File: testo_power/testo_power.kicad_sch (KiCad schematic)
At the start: 0 parts

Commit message: Test commit for KiCad schemes
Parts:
- added J1: USB_C_Receptacle_PowerOnly_6P, symbol Connector:USB_C_Receptacle_PowerOnly_6P
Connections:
- new net: J1.A12 (GND), J1.B12 (GND)
- new net: J1.A9 (VBUS), J1.B9 (VBUS)
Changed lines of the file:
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@@
 (kicad_sch
-	(version 20250114)
+	(version 20260306)
 	(generator "eeschema")
-	(generator_version "9.0")
+	(generator_version "10.0")
 	(paper "A4")
+	(symbol
+		(lib_id "Connector:USB_C_Receptacle_PowerOnly_6P")
+		(at 74.93 71.12 0)
+		(unit 1)
+		(body_style 1)
+		(exclude_from_sim no)
+		(in_bom yes)
+		(on_board yes)
+		(in_pos_files yes)
+		(dnp no)
+		(fields_autoplaced yes)
+		(property "Reference" "J1"
+			(at 74.93 53.34 0)
+			(show_name no)
+			(do_not_autoplace no)
+			(effects
+				(font
+					(size 1.27 1.27)
+				)
+			)
+		)
+		(property "Value" "USB_C_Receptacle_PowerOnly_6P"
+			(at 74.93 55.88 0)
+			(show_name no)
+			(do_not_autoplace no)
+			(effects
+				(font
+					(size 1.27 1.27)
+				)
+			)
+		)
+		(property "Footprint" ""
+			(at 78.74 68.58 0)
+			(hide yes)
+			(show_name no)
+			(do_not_autoplace no)
+			(effects
+				(font
+					(size 1.27 1.27)
+				)
+			)
+		)
+		(property "Datasheet" "https://www.usb.org/sites/default/files/documents/usb_type-c.zip"
+			(at 74.93 71.12 0)
+			(hide yes)
+			(show_name no)
+			(do_not_autoplace no)
+			(effects
+				(font
+					(size 1.27 1.27)
+				)
+			)
+		)
+		(property "Description" "USB Power-Only 6P Type-C Receptacle connector"
+			(at 74.93 71.12 0)
+			(hide yes)
+			(show_name no)
+			(do_not_autoplace no)
+			(effects
+				(font
+					(size 1.27 1.27)
+				)
+			)
+		)
+		(pin "B5"
+		)
+		(pin "A9"
+		)
+		(pin "SH"
+		)
+		(pin "A5"
+		)
+		(pin "B12"
+		)
+		(pin "A12"
+		)
+		(pin "B9"
+		)
+		(instances
+			(project "testo_power"
+				(path "/7d8517b7-4e53-4e94-8436-66e52bec9654"
+					(reference "J1")
+					(unit 1)
+				)
+			)
+		)
+	)
 	(sheet_instances
 		(path "/"

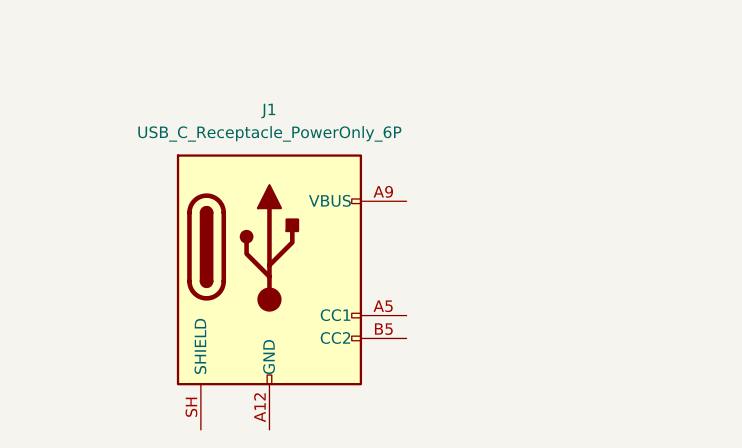
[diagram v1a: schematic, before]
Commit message: First schematic drawing
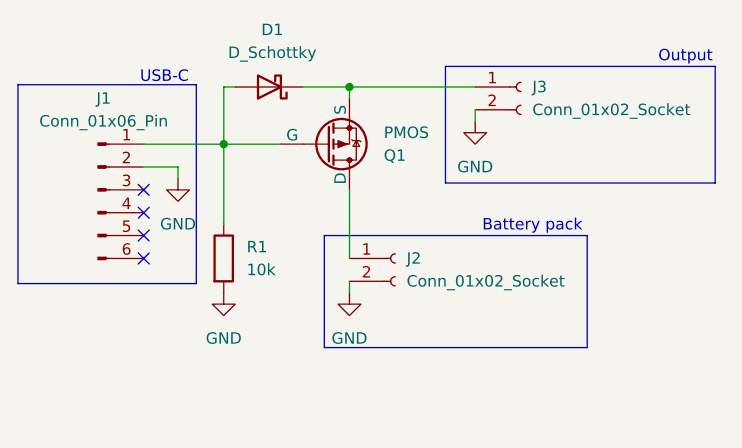
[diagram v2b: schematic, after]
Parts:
- removed J1: USB_C_Receptacle_PowerOnly_6P, symbol Connector:USB_C_Receptacle_PowerOnly_6P
- added D1: D_Schottky, symbol Device:D_Schottky
- added J1: Conn_01x06_Pin, symbol Connector:Conn_01x06_Pin
- added J2, J3: Conn_01x02_Socket, symbol Connector:Conn_01x02_Socket
- added Q1: PMOS, symbol Simulation_SPICE:PMOS
- added R1: 10k, symbol Device:R
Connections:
- new net: D1.2 (A), J1.1 (Pin_1), Q1.2 (G), R1.1
- new net: D1.1 (K), J3.1 (Pin_1), Q1.3 (S)
- new net: J2.1 (Pin_1), Q1.1 (D)
- new net GND: J1.2 (Pin_2), J2.2 (Pin_2), J3.2 (Pin_2), R1.2
- no-connect marks 0 -> 4
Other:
- note added: "Battery pack"
- note added: "Output"
- note added: "USB-C"

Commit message: First version of PCB design
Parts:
- removed Q1: PMOS, symbol Simulation_SPICE:PMOS
- added Q2: FQP27P06, Package_TO_SOT_THT:TO-220-3_Vertical, symbol Transistor_FET:FQP27P06
- D1: footprint (none) -> Diode_THT:D_5W_P10.16mm_Horizontal
- J1: footprint (none) -> Connector_PinHeader_2.54mm:PinHeader_1x06_P2.54mm_Vertical
- J2: footprint (none) -> Connector_Molex:Molex_KK-254_AE-6410-02A_1x02_P2.54mm_Vertical
- J3: footprint (none) -> Connector_PinHeader_2.54mm:PinHeader_1x02_P2.54mm_Vertical
- R1: footprint (none) -> Resistor_THT:R_Axial_DIN0207_L6.3mm_D2.5mm_P7.62mm_Horizontal
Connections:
- net V_USB: now reaches D1.2 (A), J1.1 (Pin_1), R1.1
- net V_USB: now also Q2.1 (G)
- net V_OUT: now reaches D1.1 (K), J3.1 (Pin_1)
- net V_OUT: now also Q2.3 (S)
- net V_BAT: now reaches J2.1 (Pin_1)
- net V_BAT: now also Q2.2 (D)
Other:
- moved on the sheet: J3

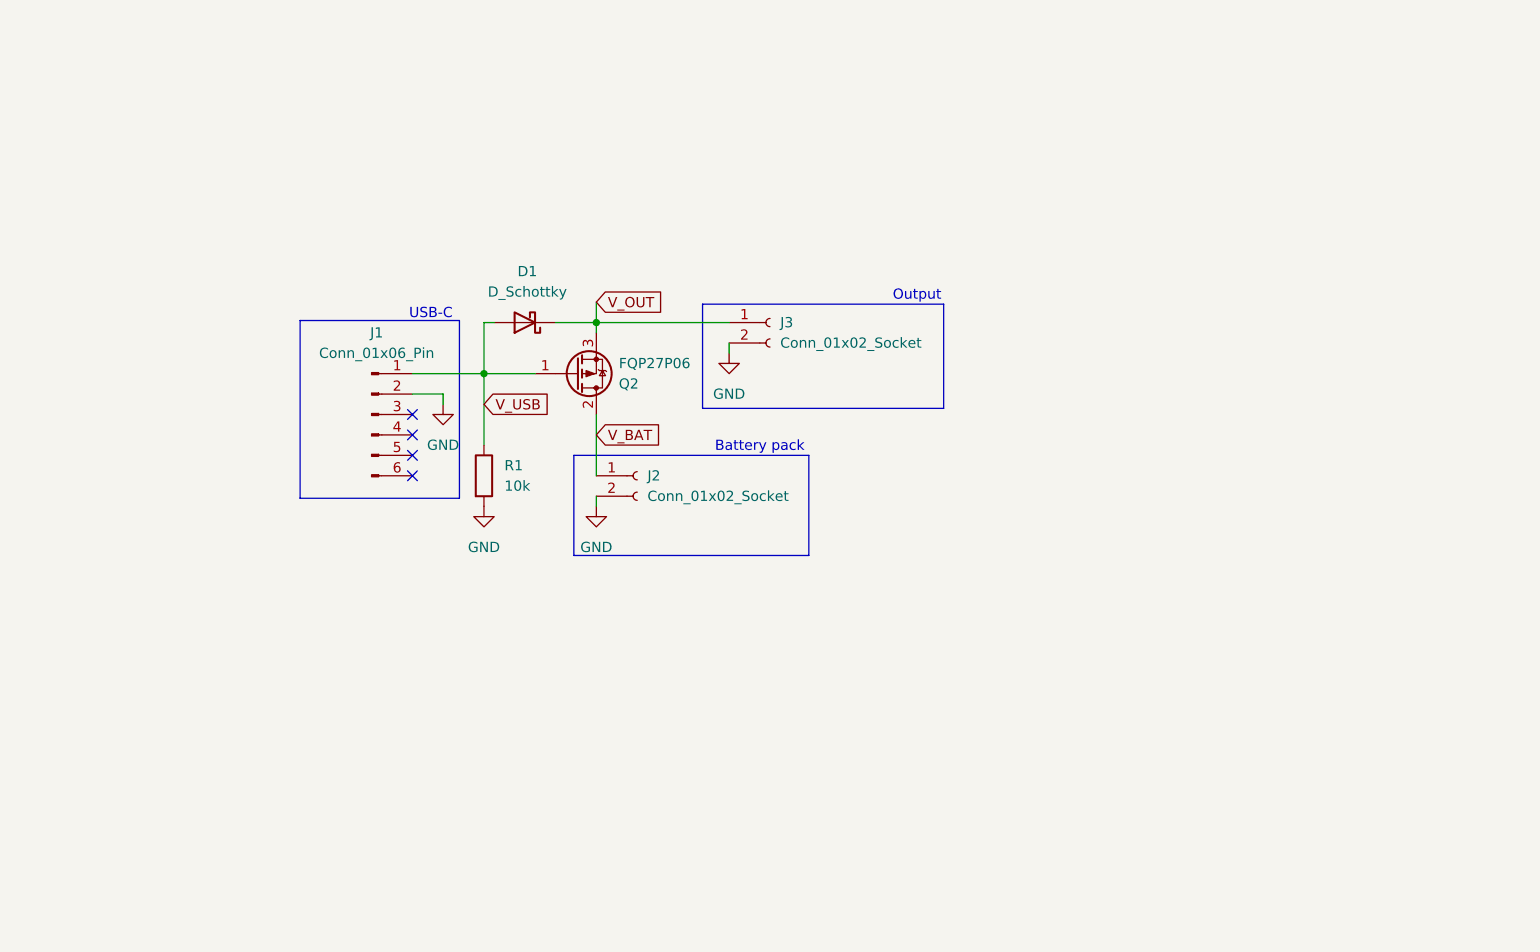
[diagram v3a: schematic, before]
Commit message: Added mounting holes, added descriptions on silkscreen, added USB power indication LED.
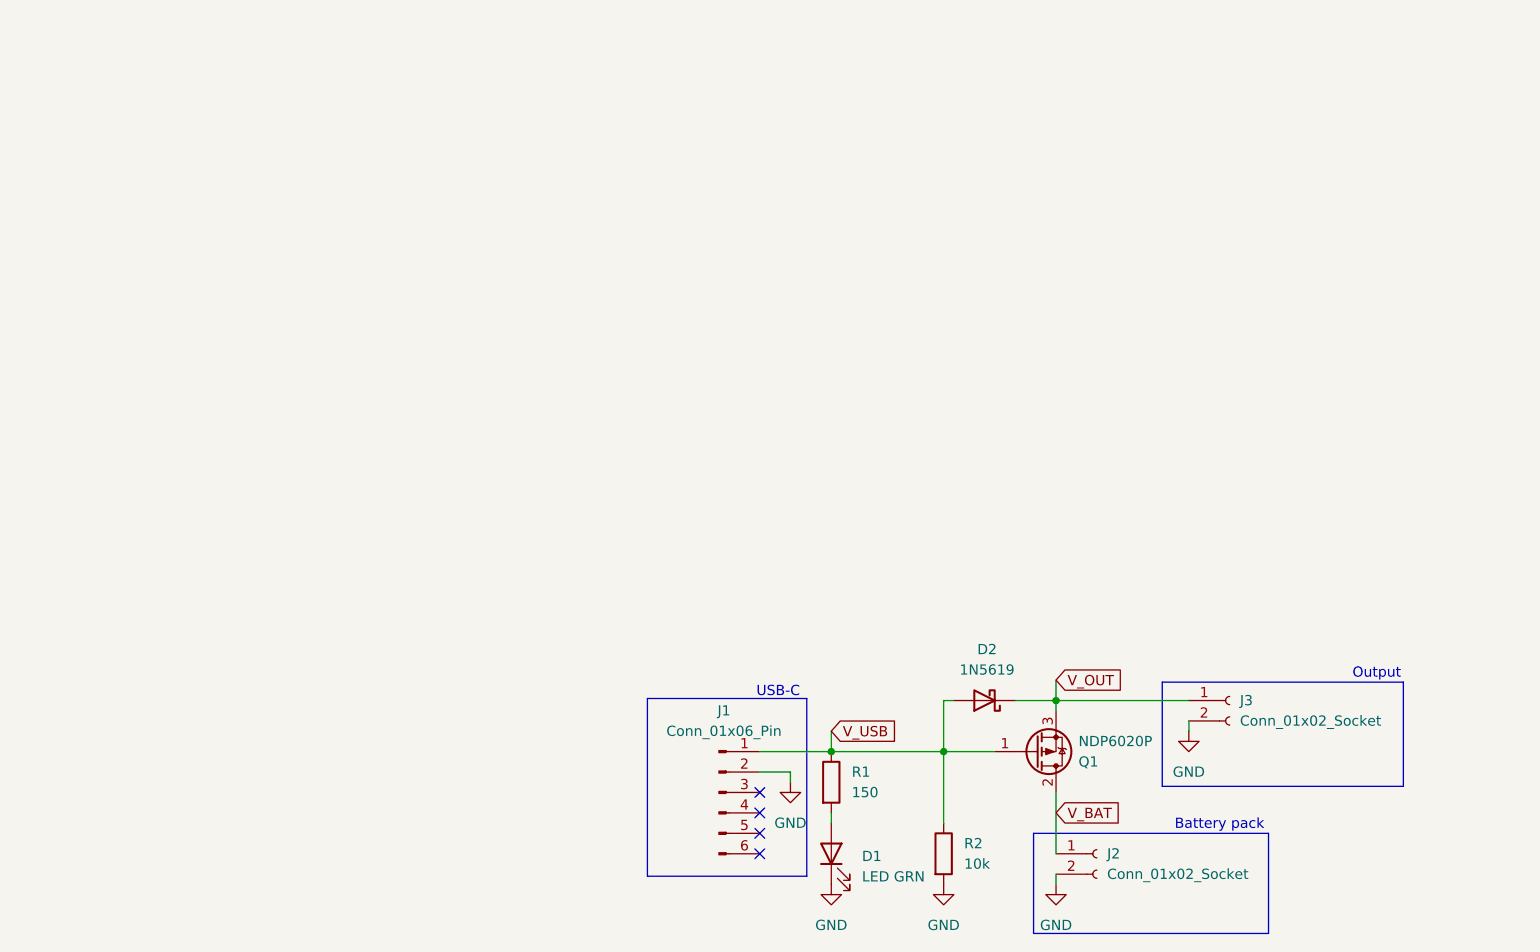
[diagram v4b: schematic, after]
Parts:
- added D1: LED GRN, LED_THT:LED_D4.0mm, symbol Device:LED
- added R1: 150, Resistor_THT:R_Axial_DIN0207_L6.3mm_D2.5mm_P7.62mm_Horizontal, symbol Device:R
- D2: renamed from D1; value D_Schottky -> 1N5619
- Q1: renamed from Q2; value FQP27P06 -> NDP6020P
- renumbered R1 to R2
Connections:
- net GND: now also D1.1 (K)
- net V_USB: now also R1.1
- new net: D1.2 (A), R1.2
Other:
- company: (none) -> Hogeschool Utrecht
- title: (none) -> Testo USB-C mod
- moved on the sheet: D2, J1, J2, J3, Q1, R2

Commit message: pcb and schematic done
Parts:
- removed J1: Conn_01x06_Pin, Connector_PinHeader_2.54mm:PinHeader_1x06_P2.54mm_Vertical, symbol Connector:Conn_01x06_Pin
- removed Q1: NDP6020P, Package_TO_SOT_THT:TO-220-3_Vertical, symbol Transistor_FET:FQP27P06
- added J1: USB_C_Receptacle_PowerOnly_6P, Connector_USB:USB_C_Receptacle_HCTL_HC-TYPE-C-16P-01A, symbol Connector:USB_C_Receptacle_PowerOnly_6P
- added Q2: IRLML6402TRPBF, Package_TO_SOT_SMD:SOT-23, symbol Transistor_FET:Q_PMOS_GSD
- added R3: 150R, Resistor_SMD:R_0603_1608Metric, symbol Device:R
- added R4: 10k, Resistor_SMD:R_0603_1608Metric, symbol Device:R
- D1: value LED GRN -> LED RED; footprint LED_THT:LED_D4.0mm -> LED_SMD:LED_0603_1608Metric; JLC Part# (none) -> C2286
- D2: value 1N5619 -> SS14; footprint Diode_THT:D_5W_P10.16mm_Horizontal -> Diode_SMD:D_SMA; JLC Part# (none) -> C2480
- J2: footprint Connector_Molex:Molex_KK-254_AE-6410-02A_1x02_P2.54mm_Vertical -> Connector_Molex:Molex_CLIK-Mate_502382-0270_1x02-1MP_P1.25mm_Vertical; JLC Part# (none) -> C27543
- J3: footprint Connector_PinHeader_2.54mm:PinHeader_1x02_P2.54mm_Vertical -> Connector_Molex:Molex_KK-254_AE-6410-02A_1x02_P2.54mm_Vertical; JLC Part# (none) -> C27543
- R1: value 150 -> 5k1; footprint Resistor_THT:R_Axial_DIN0207_L6.3mm_D2.5mm_P7.62mm_Horizontal -> Resistor_SMD:R_0603_1608Metric; JLC Part# (none) -> C23186
- R2: value 10k -> 5k1; footprint Resistor_THT:R_Axial_DIN0207_L6.3mm_D2.5mm_P7.62mm_Horizontal -> Resistor_SMD:R_0603_1608Metric; JLC Part# (none) -> C23186
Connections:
- net GND: now also R1.1, R2.1, J1.A12 (GND), J1.B12 (GND), J1.SH (SHIELD), R4.2; no longer R2.2
- net V_BAT: now also J3.1 (Pin_1), Q2.2 (S); no longer J2.1 (Pin_1)
- net V_OUT: now also J2.1 (Pin_1), Q2.3 (D); no longer J3.1 (Pin_1)
- net at D1.2 (A): now also R3.2; no longer R1.2
- removed net V_USB: D2.2 (A), R1.1, R2.1
- new net: J1.A5 (CC1), R2.2
- new net: J1.B5 (CC2), R1.2
- new net V_BUS: D2.2 (A), J1.A9 (VBUS), J1.B9 (VBUS), Q2.1 (G), R3.1, R4.1
- no-connect marks 4 -> 0
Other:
- note removed: "USB-C"

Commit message: replaced connectors
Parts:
- J2: footprint Connector_Molex:Molex_CLIK-Mate_502382-0270_1x02-1MP_P1.25mm_Vertical -> Connector_PinHeader_2.54mm:PinHeader_1x02_P2.54mm_Vertical; JLC Part# C27543 -> (none)
- J3: footprint Connector_Molex:Molex_KK-254_AE-6410-02A_1x02_P2.54mm_Vertical -> Connector_Molex:Molex_CLIK-Mate_502382-0270_1x02-1MP_P1.25mm_Vertical
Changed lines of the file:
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@@
 			)
 		)
-		(property "Footprint" "Connector_Molex:Molex_CLIK-Mate_502382-0270_1x02-1MP_P1.25mm_Vertical"
+		(property "Footprint" "Connector_PinHeader_2.54mm:PinHeader_1x02_P2.54mm_Vertical"
 			(at 176.53 59.69 0)
 			(hide yes)
@@
 			)
 		)
-		(property "Datasheet" "https://www.molex.com/content/dam/molex/molex-dot-com/products/automated/en-us/salesdrawingpdf/532/53261/532614002_sd.pdf?inline"
+		(property "Datasheet" ""
 			(at 176.53 59.69 0)
 			(hide yes)
@@
 			)
 		)
-		(property "JLC Part#" "C27543"
+		(property "JLC Part#" ""
 			(at 176.53 59.69 0)
 			(hide yes)
@@
 			)
 		)
-		(property "Footprint" "Connector_Molex:Molex_KK-254_AE-6410-02A_1x02_P2.54mm_Vertical"
+		(property "Footprint" "Connector_Molex:Molex_CLIK-Mate_502382-0270_1x02-1MP_P1.25mm_Vertical"
 			(at 176.53 76.2 0)
 			(hide yes)
@@
 			)
 		)
-		(property "Datasheet" ""
+		(property "Datasheet" "https://www.molex.com/content/dam/molex/molex-dot-com/products/automated/en-us/salesdrawingpdf/532/53261/532614002_sd.pdf?inline"
 			(at 176.53 76.2 0)
 			(hide yes)

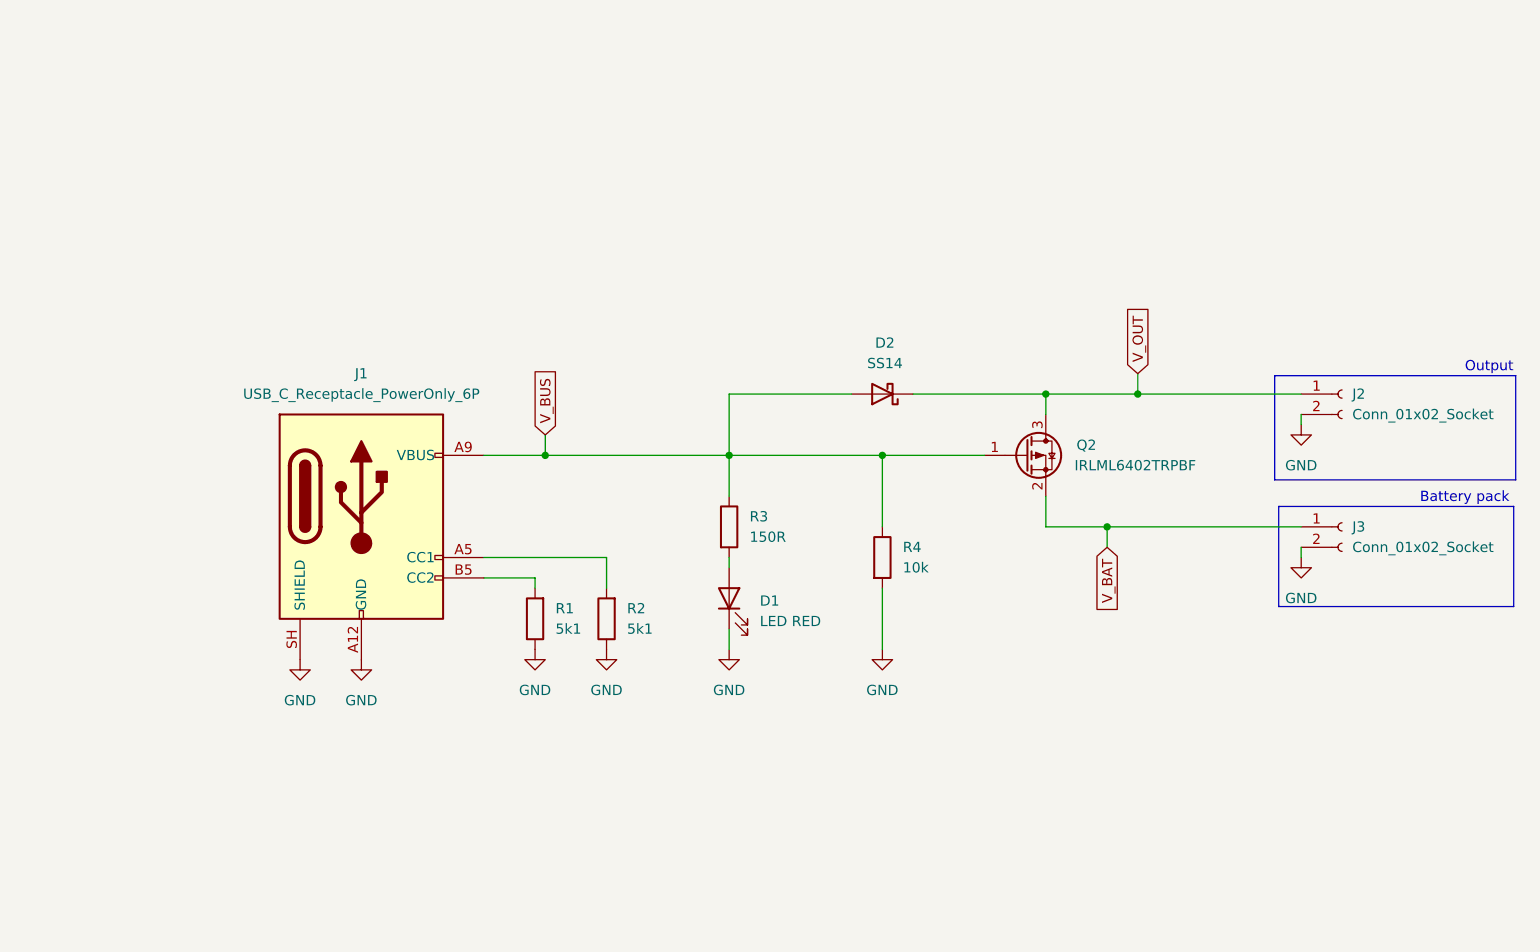
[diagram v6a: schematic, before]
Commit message: formatted schematic and added battery charger
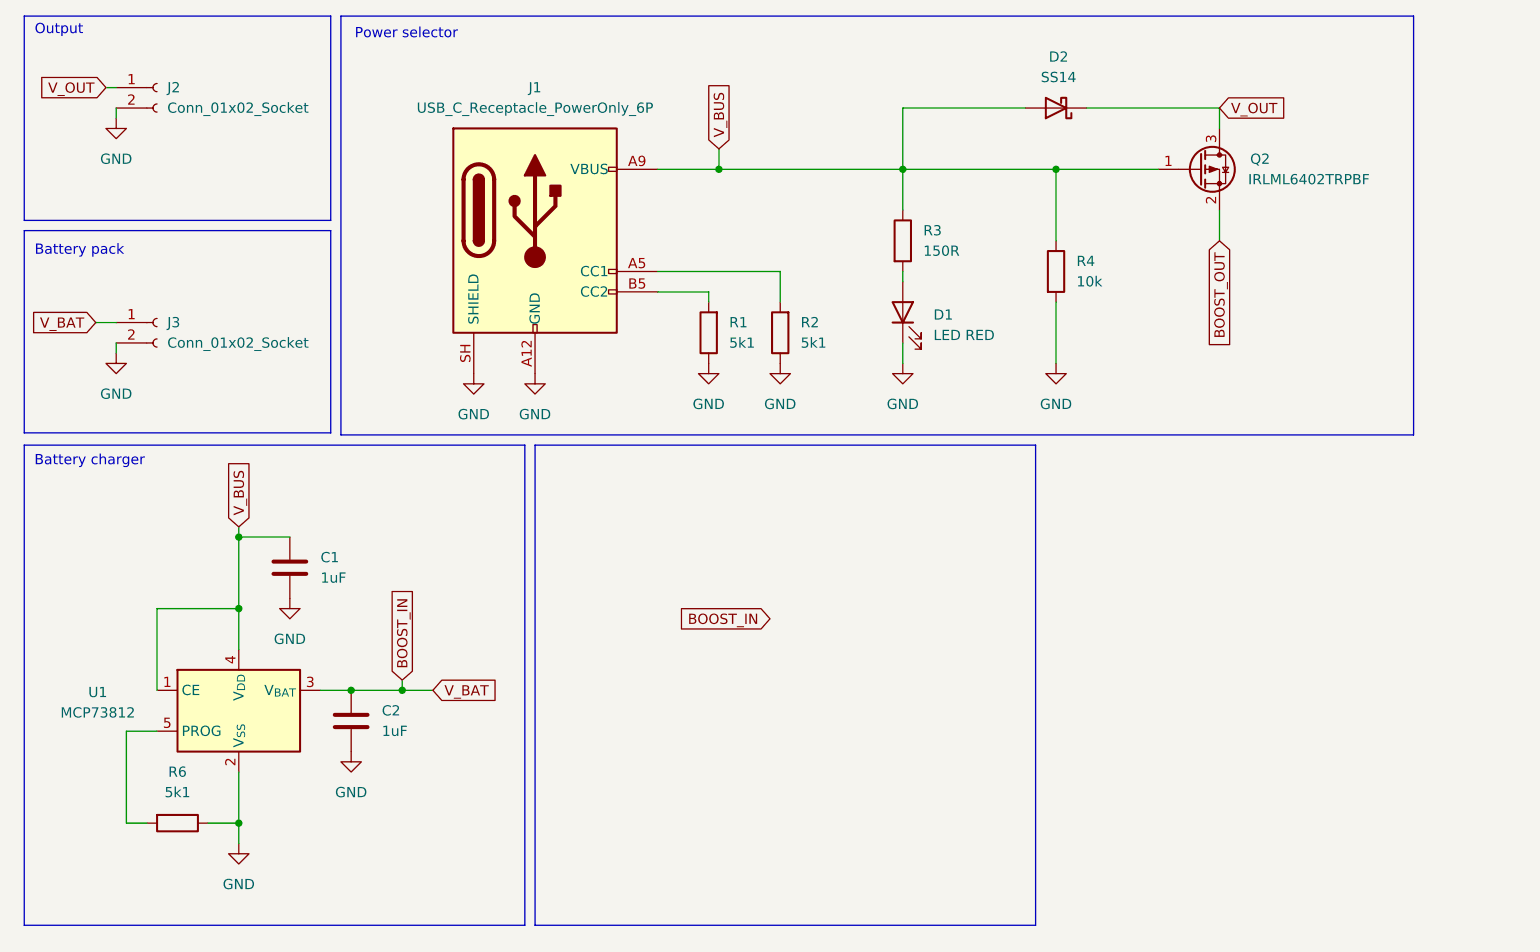
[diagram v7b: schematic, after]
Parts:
- added C1, C2: 1uF, symbol Device:C
- added R6: 5k1, Resistor_SMD:R_0603_1608Metric, symbol Device:R
- added U1: MCP73812, Package_TO_SOT_SMD:SOT-23-5, symbol Battery_Management:MCP73811T-420I-OT
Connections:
- net GND: now also C1.2, C2.2, R6.1, U1.2 (V_{SS})
- net V_BUS: now also C1.1, U1.1 (CE), U1.4 (V_{DD})
- net V_BAT renamed BOOST_IN
- net BOOST_IN: now also C2.1, U1.3 (V_{BAT}); no longer Q2.2 (S)
- new net: R6.2, U1.5 (PROG)
- new net BOOST_OUT: Q2.2 (S)
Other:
- note added: "Battery charger"
- note added: "Power selector"
- moved on the sheet: D1, D2, J1, J2, J3, Q2, R1, R2, R3, R4

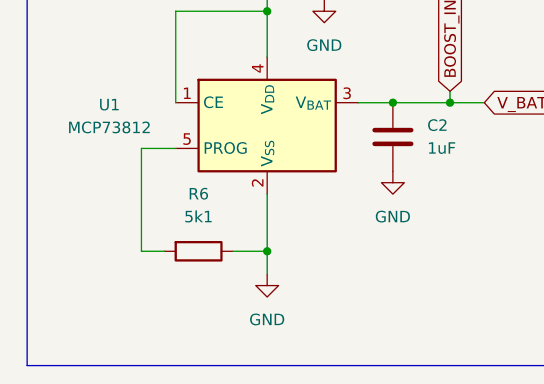
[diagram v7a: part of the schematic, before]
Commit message: added comment for charge current
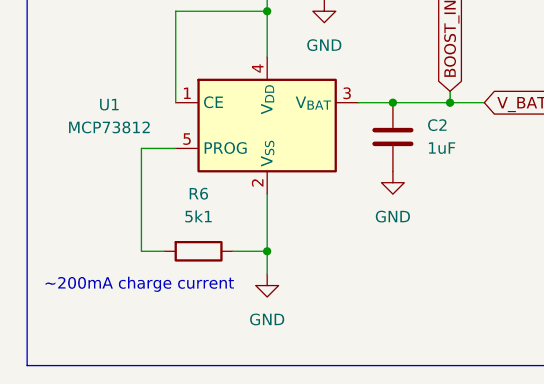
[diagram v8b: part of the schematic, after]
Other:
- note added: "~200mA charge current"
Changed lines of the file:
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@@
+		)
+	)
+	(text "~200mA charge current"
+		(exclude_from_sim no)
+		(at 25.146 116.84 0)
+		(effects
+			(font
+				(size 1.27 1.27)
+			)
 		)
 	)
